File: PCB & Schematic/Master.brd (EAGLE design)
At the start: 101.6 x 53.3 mm, 20 parts, among them M1 ARDUINO_R3_ICSP_NODIM, X1 MAB5SH, X2 MAB5SH

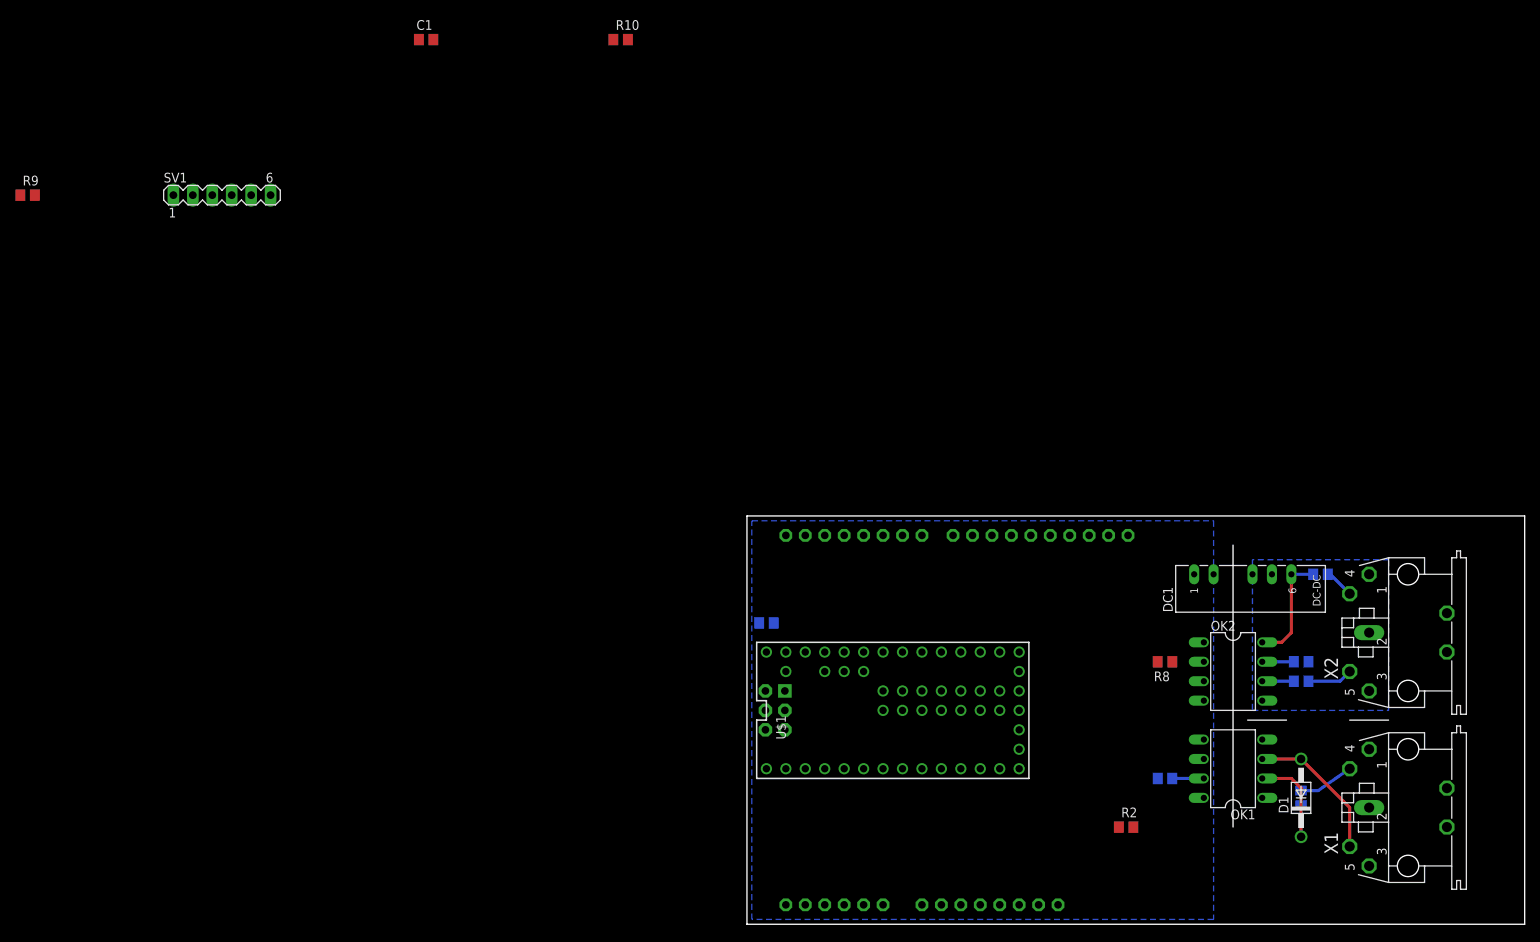
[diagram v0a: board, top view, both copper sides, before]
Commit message: Finish master PCB layout.
I should verify the watchdog and power supply work as claimed
before ordering a PCB, though.
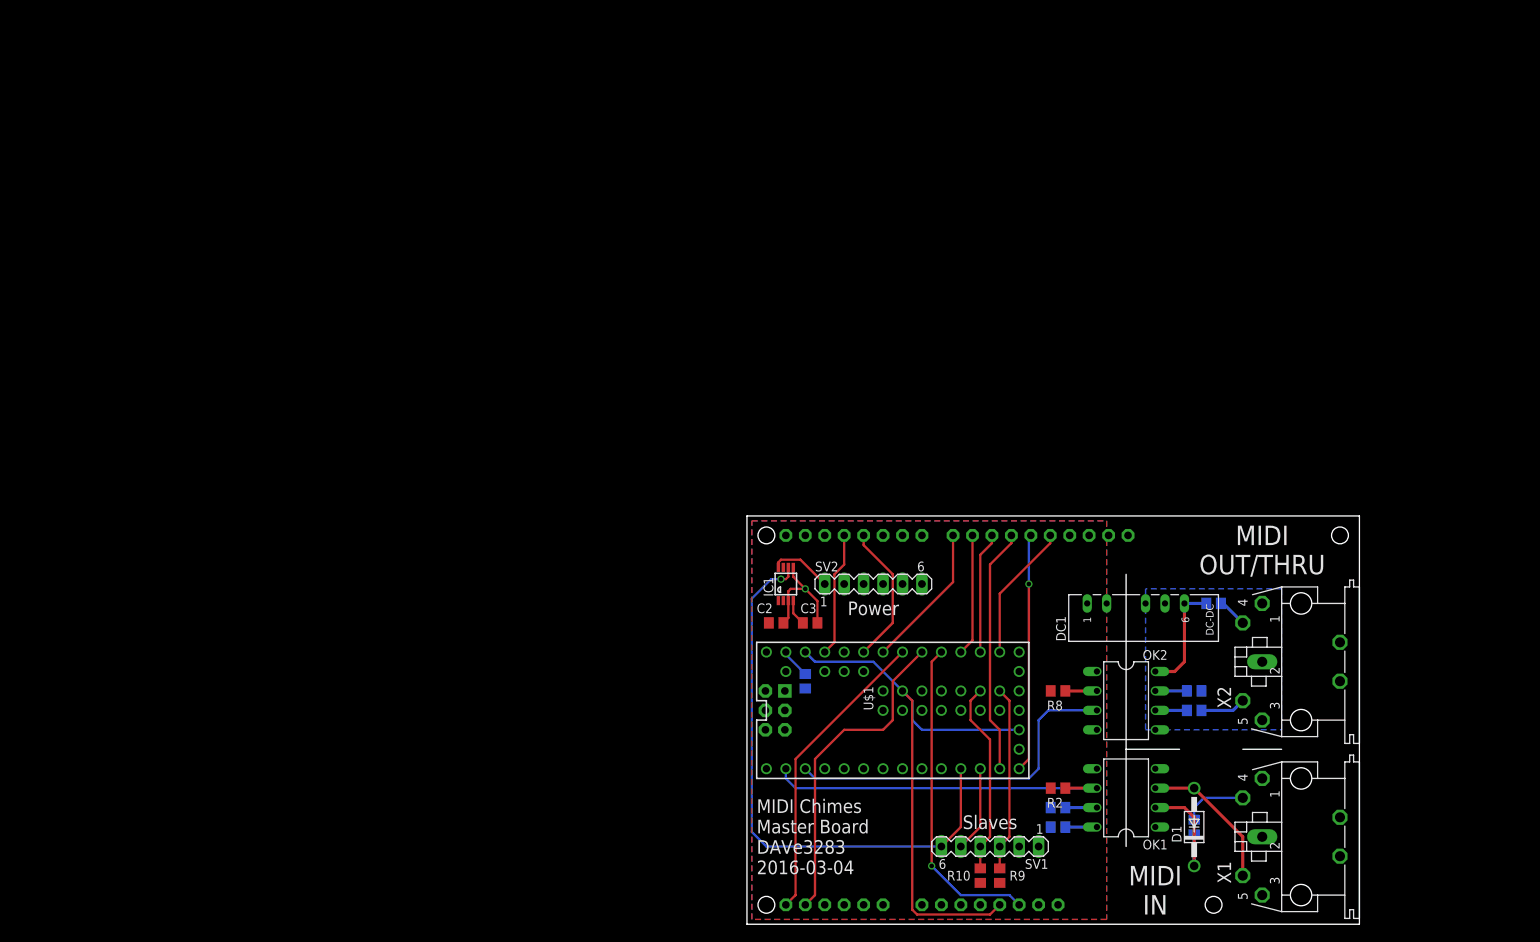
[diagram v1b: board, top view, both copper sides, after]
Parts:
- added C2: 0.1u, resistor:C0805
- added C3: 10n, resistor:C0805
- added IC1: MAX705CUA, maxim:UMAX8
- added SV2: Power Supply, con-lstb:MA06-1
- moved R9 155.0 mm to (33.0, 6.35), turned to 90 degrees
- moved C1 131.9 mm to (40.6, 12.7), flipped to the bottom
- moved SV1 131.6 mm to (31.8, 10.2), turned to 180 degrees
- moved R10 118.9 mm to (30.5, 6.35), turned to 90 degrees
- moved R5 14.5 mm to (61.0, 41.9)
- moved D1 14.5 mm to (58.4, 12.7)
- moved DC1 14.5 mm to (50.8, 41.9)
- moved OK2 14.5 mm to (49.5, 29.2)
- moved R4 14.5 mm to (58.4, 12.7)
- moved X2 14.5 mm to (72.4, 34.3)
- moved OK1 14.5 mm to (49.5, 16.5)
- moved R3 14.5 mm to (40.6, 15.2)
- moved R6 14.5 mm to (58.4, 27.9)
- moved R7 14.5 mm to (58.4, 30.5)
- moved R8 14.5 mm to (40.6, 30.5)
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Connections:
- new net N$11: IC1.8, SV2.1
- new net N$15: C3.1, IC1.4
- net +5V: now also C2.1, IC1.1, IC1.2, SV2.3
- net ADDR_LATCH: now also U$1.10; no longer U$1.3
- net GND: now also C2.2, C3.2, IC1.3, IC1.5, SV2.2, SV2.4
- net LCD_BACKLIGHT: now also U$1.23/A9; no longer U$1.4
- net LCD_CS: now also U$1.15/A1; no longer U$1.10
- net LCD_DC: now also U$1.16/A2; no longer U$1.9
- net LCD_RESET: now also U$1.17/A3; no longer U$1.16/A2
- net PS_EN: now also IC1.6, U$1.9; no longer U$1.2
- net SD_CARD_CS: now also U$1.21/A7; no longer U$1.15/A1
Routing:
- net +3V3: track 0.00 -> 75.0 mm
- net PS_EN: track 0.00 -> 74.4 mm, vias 0 -> 1
- net MIDI_IN: track 0.00 -> 46.6 mm
- net MIDI_OUT: track 0.00 -> 46.0 mm
- net TOUCH_SDA: track 0.00 -> 42.3 mm
- net LCD_RESET: track 0.00 -> 42.0 mm, vias 0 -> 1
- net TOUCH_SCL: track 0.00 -> 39.3 mm
- net SPI_MOSI: track 0.00 -> 32.2 mm
- net SPI_MISO: track 0.00 -> 31.1 mm, vias 0 -> 1
- net I2C_SDA: track 0.00 -> 25.3 mm
- net I2C_SCL: track 0.00 -> 24.2 mm
- net TOUCH_CS: track 0.00 -> 19.0 mm
- net SD_CARD_CS: track 0.00 -> 18.4 mm
- net SPI_SCK: track 0.00 -> 18.0 mm
- net LCD_BACKLIGHT: track 0.00 -> 16.3 mm
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- added copper zone on layer 1, net +5V
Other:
- board size 101.6 x 53.3 mm -> 80 x 53.3 mm
- board text added: "MIDI Chimes Master Board DAVe3283 2016-03-04"
- board text added: "MIDI IN"
- board text added: "MIDI OUT/THRU"
- board text added: "Power"
- board text added: "Slaves"

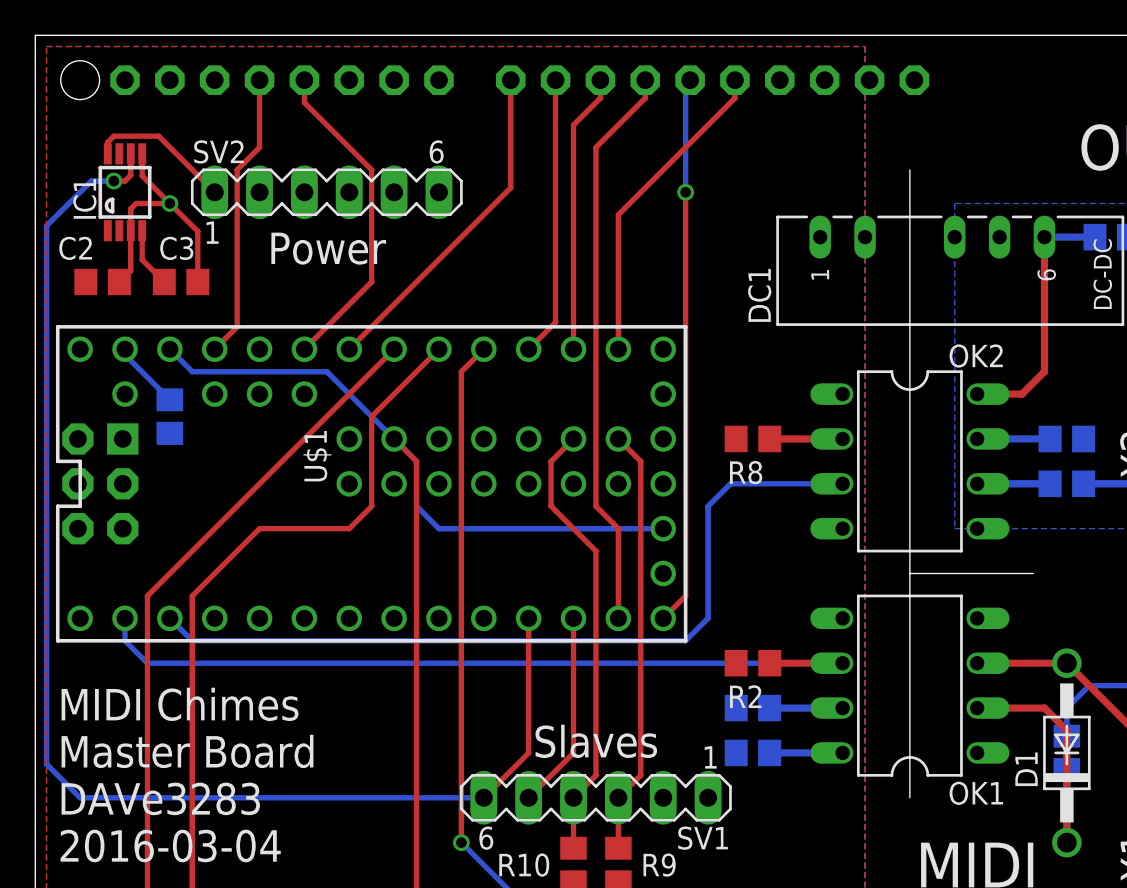
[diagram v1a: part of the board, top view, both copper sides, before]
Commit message: Make the correct part for the watchdog.
This is much cleaner.
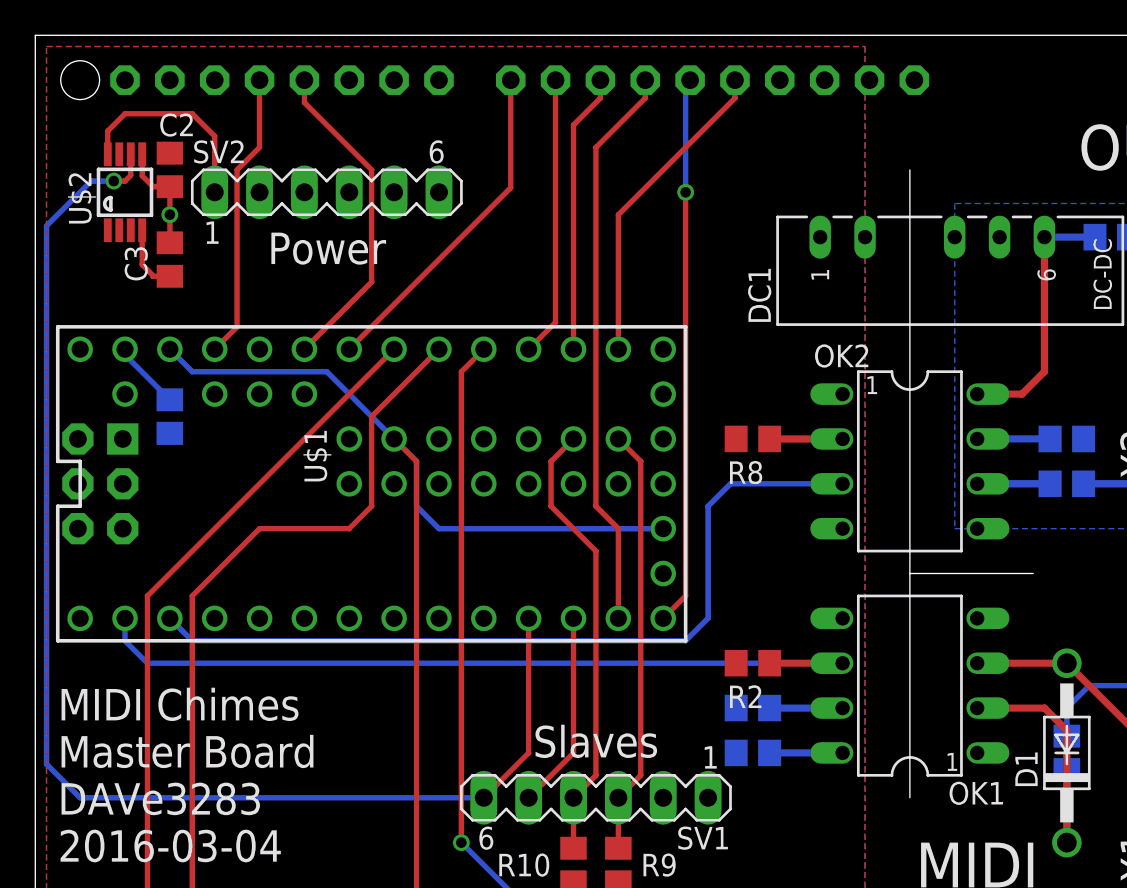
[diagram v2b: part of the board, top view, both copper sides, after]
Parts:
- removed IC1: MAX705CUA, maxim:UMAX8
- added U$2: MAX16997, DAVe3283:UMAX-U8-1
- moved C2 7.41 mm to (7.62, 45.7), turned to 270 degrees
- moved C3 1.42 mm to (7.62, 40.6), turned to 90 degrees
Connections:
- removed net N$15: C3.1, IC1.4
- new net N$8: C3.1, U$2.4
- net +5V: now also U$2.1, U$2.2; no longer IC1.1, IC1.2
- net GND: now also U$2.5; no longer IC1.3, IC1.5
- net N$11: now also U$2.8; no longer IC1.8
- net PS_EN: now also U$2.6; no longer IC1.6
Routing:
- net GND: track 15.3 -> 6.22 mm
- net N$8: track 0.00 -> 3.82 mm
- net N$15: track 3.42 -> 0.00 mm
- net N$11: track 8.17 -> 11.5 mm
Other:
- board text added: "1"
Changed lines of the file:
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@@
 <layer number="27" name="tValues" color="7" fill="1" visible="no" active="yes"/>
 <layer number="28" name="bValues" color="7" fill="1" visible="no" active="yes"/>
-<layer number="29" name="tStop" color="7" fill="3" visible="no" active="yes"/>
-<layer number="30" name="bStop" color="7" fill="6" visible="no" active="yes"/>
+<layer number="29" name="tStop" color="7" fill="3" visible="yes" active="yes"/>
+<layer number="30" name="bStop" color="7" fill="6" visible="yes" active="yes"/>
 <layer number="31" name="tCream" color="7" fill="4" visible="no" active="yes"/>
 <layer number="32" name="bCream" color="7" fill="5" visible="no" active="yes"/>
@@
 <hole x="77.47" y="50.8" drill="2.2"/>
 <hole x="60.96" y="2.54" drill="2.2"/>
+<text x="46.99" y="33.02" size="1.016" layer="25" ratio="10">1</text>
+<text x="52.324" y="12.7" size="1.016" layer="25" ratio="10" rot="R180">1</text>
 </plain>
 <attributes>
@@
 <attribute name="MPN" value="6N138" x="49.53" y="29.21" size="1.778" layer="27" rot="R270" display="off"/>
 <attribute name="OC_NEWARK" value="35K5294" x="49.53" y="29.21" size="1.778" layer="27" rot="R270" display="off"/>
-<attribute name="NAME" x="51.689" y="34.544" size="1.27" layer="25" ratio="10"/>
+<attribute name="NAME" x="44.069" y="34.544" size="1.27" layer="25" ratio="10"/>
 <attribute name="VALUE" x="48.895" y="32.766" size="1.27" layer="27" ratio="10" rot="R270"/>
 </element>
@@
 <attribute name="NAME" x="8.89" y="46.101" size="1.27" layer="25" ratio="10"/>
 </element>
-<element name="IC1" library="maxim" package="UMAX8" value="MAX705CUA" x="5.08" y="44.45" smashed="yes">
-<attribute name="OC_FARNELL" value="unknown" x="5.08" y="44.45" size="1.778" layer="27" display="off"/>
-<attribute name="MF" value="" x="5.08" y="44.45" size="1.778" layer="27" display="off"/>
-<attribute name="MPN" value="MAX705CUA+" x="5.08" y="44.45" size="1.778" layer="27" display="off"/>
-<attribute name="OC_NEWARK" value="13M2396" x="5.08" y="44.45" size="1.778" layer="27" display="off"/>
-<attribute name="NAME" x="3.444" y="42.799" size="1.27" layer="25" rot="R90"/>
-</element>
-<element name="C2" library="resistor" package="C0805" value="0.1u" x="3.81" y="39.37" smashed="yes">
-<attribute name="NAME" x="1.27" y="40.64" size="1.27" layer="25"/>
-<attribute name="VALUE" x="1.905" y="36.83" size="1.27" layer="27"/>
-</element>
-<element name="C3" library="resistor" package="C0805" value="10n" x="8.255" y="39.37"/>
+<element name="C2" library="resistor" package="C0805" value="0.1u" x="7.62" y="45.72" smashed="yes" rot="R270">
+<attribute name="NAME" x="6.985" y="47.625" size="1.27" layer="25"/>
+<attribute name="VALUE" x="9.525" y="47.625" size="1.27" layer="27"/>
+</element>
+<element name="C3" library="resistor" package="C0805" value="10n" x="7.62" y="40.64" rot="R90"/>
+<element name="U$2" library="DAVe3283" package="UMAX-U8-1" value="MAX16997" x="5.08" y="44.45" smashed="yes">
+<attribute name="MPN" value="MAX16997A" x="5.08" y="44.45" size="1.778" layer="27" display="off"/>
+<attribute name="NAME" x="3.175" y="42.545" size="1.27" layer="25" rot="R90"/>
+</element>
 </elements>
 <signals>
@@
 </polygon>
 <contactref element="SV1" pad="1"/>
+<contactref element="C2" pad="2"/>
+<contactref element="C3" pad="2"/>
 <contactref element="SV2" pad="2"/>
 <contactref element="SV2" pad="4"/>
-<contactref element="IC1" pad="3"/>
-<contactref element="IC1" pad="5"/>
-<contactref element="C2" pad="2"/>
-<contactref element="C3" pad="2"/>
-<via x="7.62" y="43.815" extent="1-16" drill="0.6" shape="square"/>
-<wire x1="6.055" y1="46.625" x2="6.055" y2="45.38" width="0.3048" layer="1"/>
-<wire x1="6.055" y1="45.38" x2="7.62" y2="43.815" width="0.3048" layer="1"/>
-<wire x1="5.405" y1="42.275" x2="5.405" y2="40.015" width="0.3048" layer="1"/>
-<wire x1="5.405" y1="40.015" x2="4.76" y2="39.37" width="0.3048" layer="1"/>
-<wire x1="9.205" y1="39.37" x2="9.205" y2="42.23" width="0.3048" layer="1"/>
-<wire x1="9.205" y1="42.23" x2="7.62" y2="43.815" width="0.3048" layer="1"/>
-<wire x1="5.405" y1="42.275" x2="5.405" y2="43.505" width="0.3048" layer="1"/>
-<wire x1="5.405" y1="43.505" x2="5.715" y2="43.815" width="0.3048" layer="1"/>
-<wire x1="5.715" y1="43.815" x2="7.62" y2="43.815" width="0.3048" layer="1"/>
+<contactref element="U$2" pad="5"/>
+<via x="7.62" y="43.18" extent="1-16" drill="0.6" shape="square"/>
+<wire x1="6.055" y1="46.6" x2="6.055" y2="45.38" width="0.3048" layer="1"/>
+<wire x1="7.62" y1="44.77" x2="6.665" y2="44.77" width="0.3048" layer="1"/>
+<wire x1="6.665" y1="44.77" x2="6.055" y2="45.38" width="0.3048" layer="1"/>
+<wire x1="7.62" y1="43.18" x2="7.62" y2="44.77" width="0.3048" layer="1"/>
+<wire x1="7.62" y1="41.59" x2="7.62" y2="43.18" width="0.3048" layer="1"/>
 </signal>
 <signal name="VIN">
@@
 <contactref element="SV2" pad="3"/>
 <contactref element="C2" pad="1"/>
-<contactref element="IC1" pad="1"/>
-<contactref element="IC1" pad="2"/>
 <polygon width="0.3048" layer="1" isolate="0.254">
 <vertex x="0.635" y="52.705"/>
@@
 <vertex x="0.635" y="0.635"/>
 </polygon>
+<contactref element="U$2" pad="1"/>
+<contactref element="U$2" pad="2"/>
 </signal>
 <signal name="AGND">
@@
 <signal name="PS_EN">
 <contactref element="SV1" pad="6"/>
-<contactref element="IC1" pad="6"/>
 <contactref element="U$1" pad="9"/>
-<wire x1="5.405" y1="46.625" x2="5.405" y2="45.41" width="0.3048" layer="1"/>
 <wire x1="5.405" y1="45.41" x2="5.08" y2="45.085" width="0.3048" layer="1"/>
 <wire x1="5.08" y1="45.085" x2="4.445" y2="45.085" width="0.3048" layer="1"/>
@@
 <wire x1="0.635" y1="42.545" x2="0.635" y2="12.065" width="0.3048" layer="16"/>
 <wire x1="0.635" y1="12.065" x2="2.54" y2="10.16" width="0.3048" layer="16"/>
+<contactref element="U$2" pad="6"/>
+<wire x1="5.405" y1="46.6" x2="5.405" y2="45.41" width="0.3048" layer="1"/>
 </signal>
 <signal name="ADDR_LATCH">
@@
 <wire x1="60.01" y1="41.91" x2="57.15" y2="41.91" width="0.4064" layer="16"/>
 </signal>
-<signal name="N$15">
+<signal name="N$11">
+<contactref element="SV2" pad="1"/>
+<contactref element="U$2" pad="8"/>
+<wire x1="4.105" y1="46.6" x2="4.105" y2="47.92" width="0.3048" layer="1"/>
+<wire x1="4.105" y1="47.92" x2="5.08" y2="48.895" width="0.3048" layer="1"/>
+<wire x1="5.08" y1="48.895" x2="8.89" y2="48.895" width="0.3048" layer="1"/>
+<wire x1="8.89" y1="48.895" x2="10.16" y2="47.625" width="0.3048" layer="1"/>
+<wire x1="10.16" y1="47.625" x2="10.16" y2="44.45" width="0.3048" layer="1"/>
+</signal>
+<signal name="N$8">
+<contactref element="U$2" pad="4"/>
 <contactref element="C3" pad="1"/>
-<contactref element="IC1" pad="4"/>
-<wire x1="6.055" y1="42.275" x2="6.055" y2="40.62" width="0.3048" layer="1"/>
-<wire x1="6.055" y1="40.62" x2="7.305" y2="39.37" width="0.3048" layer="1"/>
-</signal>
-<signal name="N$11">
-<contactref element="IC1" pad="8"/>
-<contactref element="SV2" pad="1"/>
-<wire x1="4.105" y1="46.625" x2="4.105" y2="47.285" width="0.3048" layer="1"/>
-<wire x1="4.105" y1="47.285" x2="4.445" y2="47.625" width="0.3048" layer="1"/>
-<wire x1="4.445" y1="47.625" x2="6.985" y2="47.625" width="0.3048" layer="1"/>
-<wire x1="10.16" y1="44.45" x2="6.985" y2="47.625" width="0.3048" layer="1"/>
+<wire x1="6.055" y1="42.3" x2="6.055" y2="40.345" width="0.3048" layer="1"/>
+<wire x1="7.62" y1="39.69" x2="6.665" y2="39.69" width="0.3048" layer="1"/>
+<wire x1="6.665" y1="39.69" x2="6.665" y2="39.735" width="0.3048" layer="1"/>
+<wire x1="6.665" y1="39.735" x2="6.055" y2="40.345" width="0.3048" layer="1"/>
 </signal>
 </signals>
